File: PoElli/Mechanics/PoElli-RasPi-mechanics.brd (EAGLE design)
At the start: 85 x 56 mm, 30 parts, among them J1 DF12-ELLI-HEADER-TOP, J3 M022.54MM, J4 M022.54MM, T1 Coilcraft 230NL, T2 FLYBACK750311689, U3 FST3257, X1 M-BOLT-2, X2 M-BOLT-2, X3 M-BOLT-2, X4 M-BOLT-2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

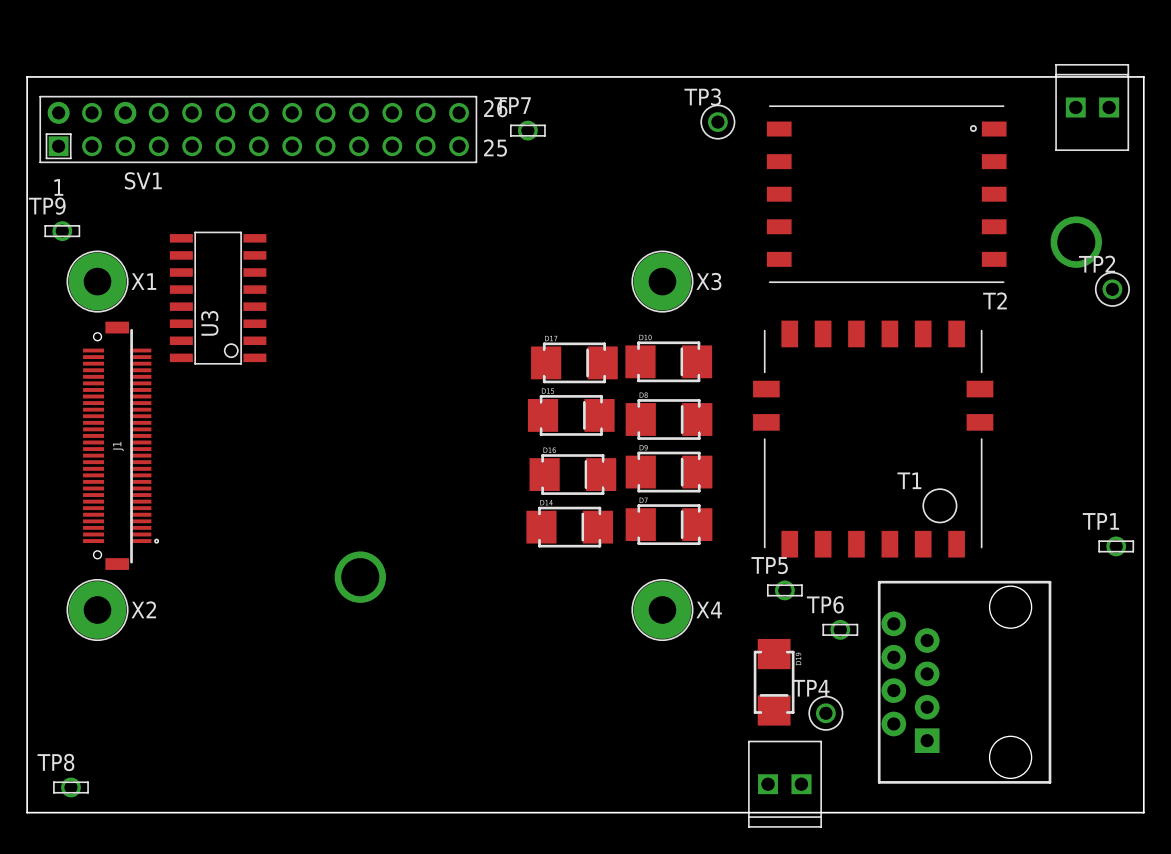
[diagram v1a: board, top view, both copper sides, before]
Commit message: Update RasPi outline & connector
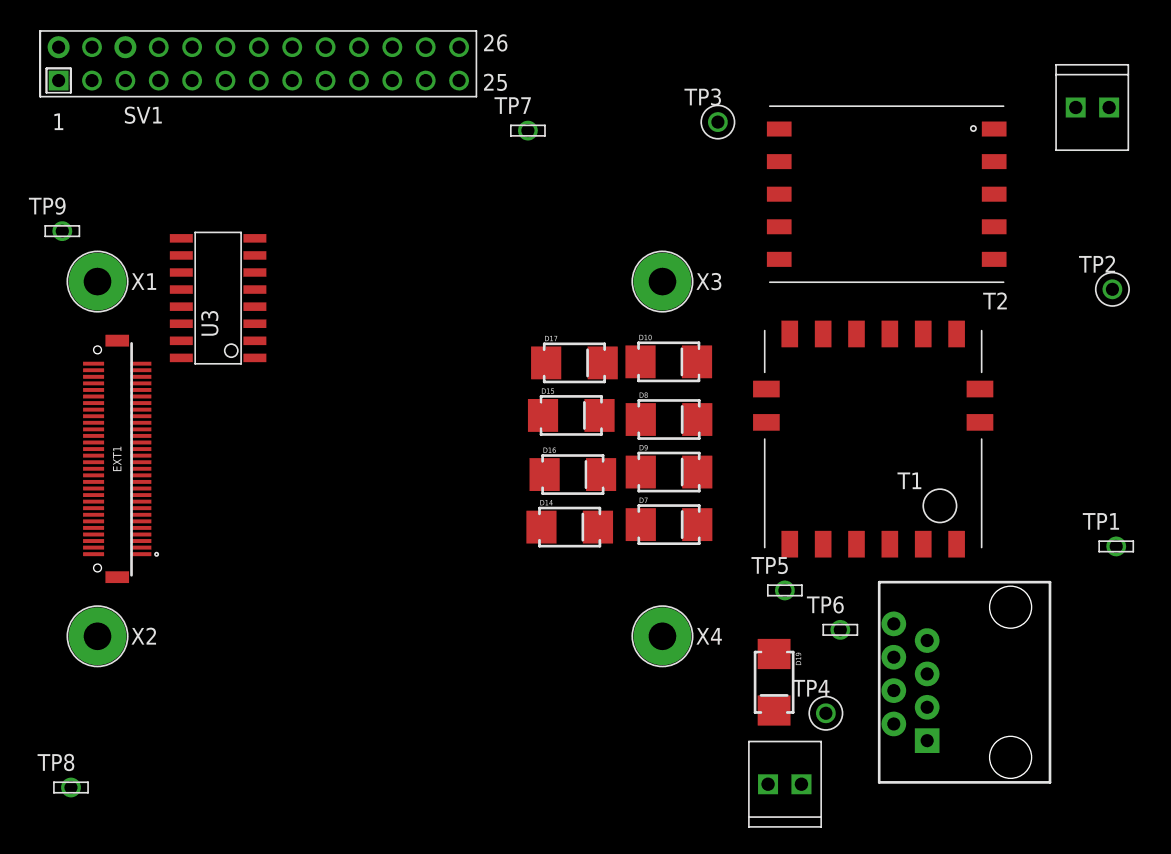
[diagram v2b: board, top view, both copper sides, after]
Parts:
- removed J1: DF12-ELLI-HEADER-TOP, ELL-i-Connectors:DF12(4.0)-60DP-0.5V
- added EXT1: DF12-ELLI-HEADER-TOP, ELL-i-Connectors:DF12(4.0)-60DP-0.5V
- added OUTLINE1: RASPBERRY-OUTLINE, ELL-i-Boards:RASPBERRYPI-SHIELD-OUTLINE
- SV1: value RASPBERRY-SHIELD -> RASPBERRY-CONNECTOR; device ELL-i-Boards:RASPBERRYPI-SHIELD-FULLSIZE -> ELL-i-Boards:RASPBERRYPI-SHIELD-CONNECTOR
- moved SV1 59.8 mm to (17.8, 57.1)
- moved X2 2.00 mm to (5.50, 13.5)
- moved X4 2.00 mm to (48.5, 13.5)
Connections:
- net 3.3V: now also EXT1.6; no longer J1.6
- net 5V: now also EXT1.8; no longer J1.8
- net GND: now also EXT1.12, EXT1.14; no longer J1.12, J1.14
- net VBATT: now also EXT1.4; no longer J1.4
- net VCC(IO): now also EXT1.2; no longer J1.2
- net VIN: now also EXT1.10; no longer J1.10
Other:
- board outline removed
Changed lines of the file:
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@@
 <setting verticaltext="up"/>
 </settings>
-<grid distance="1" unitdist="mm" unit="mm" style="lines" multiple="1" display="no" altdistance="0.5" altunitdist="inch" altunit="mm"/>
+<grid distance="1" unitdist="mm" unit="mm" style="lines" multiple="1" display="no" altdistance="0.1" altunitdist="inch" altunit="inch"/>
 <layers>
 <layer number="1" name="Top" color="4" fill="1" visible="yes" active="yes"/>
@@
 <layer number="111" name="111" color="7" fill="1" visible="yes" active="yes"/>
 <layer number="112" name="tSilk" color="7" fill="1" visible="yes" active="yes"/>
+<layer number="113" name="IDFDebug" color="4" fill="1" visible="yes" active="yes"/>
 <layer number="116" name="Patch_BOT" color="9" fill="4" visible="yes" active="yes"/>
 <layer number="118" name="Rect_Pads" color="7" fill="1" visible="yes" active="yes"/>
@@
 <elements>
 <element name="T1" library="ELL-i-Transformers" package="COILCRAFT-ETH1-230L" value="Coilcraft 230NL" x="64.54" y="28.51" rot="R180"/>
-<element name="SV1" library="ELL-i-Boards" package="RASPBERRYPI-SHIELD-FULLSIZE" value="RASPBERRY-SHIELD" x="0" y="0"/>
-<element name="J1" library="ELL-i-Connectors" package="DF12(4.0)-60DP-0.5V" value="DF12-ELLI-HEADER-TOP" x="7" y="28" rot="R90"/>
+<element name="SV1" library="ELL-i-Boards" package="RASPBERRYPI-SHIELD-CONNECTOR" value="RASPBERRY-CONNECTOR" x="17.78" y="57.07"/>
+<element name="EXT1" library="ELL-i-Connectors" package="DF12(4.0)-60DP-0.5V" value="DF12-ELLI-HEADER-TOP" x="7" y="27" rot="R90"/>
 <element name="D17" library="ELL-i-DIscreteSemi" package="DIODE-B2100" value="B2100" x="41.8" y="34.31"/>
 <element name="D16" library="ELL-i-DIscreteSemi" package="DIODE-B2100" value="B2100" x="41.68" y="25.81"/>
@@
 <element name="D19" library="ELL-i-DIscreteSemi" package="DIODE-B2100" value="B2100" x="57" y="10" rot="R270"/>
 <element name="X1" library="ELL-i-Connectors" package="M2-1" value="M-BOLT-2" x="5.5" y="40.5"/>
-<element name="X2" library="ELL-i-Connectors" package="M2-1" value="M-BOLT-2" x="5.5" y="15.5"/>
+<element name="X2" library="ELL-i-Connectors" package="M2-1" value="M-BOLT-2" x="5.5" y="13.5"/>
 <element name="X3" library="ELL-i-Connectors" package="M2-1" value="M-BOLT-2" x="48.5" y="40.5"/>
-<element name="X4" library="ELL-i-Connectors" package="M2-1" value="M-BOLT-2" x="48.5" y="15.5"/>
+<element name="X4" library="ELL-i-Connectors" package="M2-1" value="M-BOLT-2" x="48.5" y="13.5"/>
 <element name="X5" library="ELL-i-Connectors" package="4UCON-04892" value="POE-TP-RJ45-4UCON" x="75" y="10" rot="R90"/>
+<element name="OUTLINE1" library="ELL-i-Boards" package="RASPBERRYPI-SHIELD-OUTLINE" value="RASPBERRY-OUTLINE" x="0" y="5"/>
 </elements>
 <signals>
 <signal name="VIN">
-<contactref element="J1" pad="10"/>
+<contactref element="EXT1" pad="10"/>
 </signal>
 <signal name="VBATT">
-<contactref element="J1" pad="4"/>
+<contactref element="EXT1" pad="4"/>
 </signal>
 <signal name="N$1">
@@
 </signal>
 <signal name="5V">
-<contactref element="J1" pad="8"/>
+<contactref element="EXT1" pad="8"/>
 <contactref element="SV1" pad="4"/>
 <contactref element="SV1" pad="2"/>
-<wire x1="2.54" y1="53.34" x2="5.08" y2="53.34" width="0" layer="19" extent="1-1"/>
-<wire x1="5.1999" y1="22.25" x2="5.08" y2="53.34" width="0" layer="19" extent="1-1"/>
+<wire x1="2.54" y1="58.34" x2="5.08" y2="58.34" width="0" layer="19" extent="1-1"/>
+<wire x1="5.1999" y1="21.25" x2="5.08" y2="58.34" width="0" layer="19" extent="1-1"/>
 </signal>
 <signal name="POE_A+">
@@
 </signal>
 <signal name="VCC(IO)">
-<contactref element="J1" pad="2"/>
+<contactref element="EXT1" pad="2"/>
 </signal>
 <signal name="GND">
-<contactref element="J1" pad="14"/>
-<contactref element="J1" pad="12"/>
+<contactref element="EXT1" pad="14"/>
+<contactref element="EXT1" pad="12"/>
 <contactref element="U3" pad="8"/>
 <contactref element="SV1" pad="9"/>
@@
 <contactref element="SV1" pad="14"/>
 <contactref element="SV1" pad="6"/>
-<wire x1="25.4" y1="53.34" x2="33.02" y2="50.8" width="0" layer="19" extent="1-1"/>
-<wire x1="17.78" y1="53.34" x2="25.4" y2="53.34" width="0" layer="19" extent="1-1"/>
-<wire x1="12.7" y1="50.8" x2="17.78" y2="53.34" width="0" layer="19" extent="1-1"/>
-<wire x1="7.62" y1="53.34" x2="12.7" y2="50.8" width="0" layer="19" extent="1-1"/>
-<wire x1="17.48" y1="43.79" x2="12.7" y2="50.8" width="0" layer="19" extent="1-1"/>
-<wire x1="5.1999" y1="23.75" x2="17.48" y2="43.79" width="0" layer="19" extent="1-1"/>
-<wire x1="5.1999" y1="23.25" x2="5.1999" y2="23.75" width="0" layer="19" extent="1-1"/>
+<wire x1="25.4" y1="58.34" x2="33.02" y2="55.8" width="0" layer="19" extent="1-1"/>
+<wire x1="17.78" y1="58.34" x2="25.4" y2="58.34" width="0" layer="19" extent="1-1"/>
+<wire x1="12.7" y1="55.8" x2="17.78" y2="58.34" width="0" layer="19" extent="1-1"/>
+<wire x1="7.62" y1="58.34" x2="12.7" y2="55.8" width="0" layer="19" extent="1-1"/>
+<wire x1="17.48" y1="43.79" x2="12.7" y2="55.8" width="0" layer="19" extent="1-1"/>
+<wire x1="5.1999" y1="22.75" x2="17.48" y2="43.79" width="0" layer="19" extent="1-1"/>
+<wire x1="5.1999" y1="22.25" x2="5.1999" y2="22.75" width="0" layer="19" extent="1-1"/>
 </signal>
 <signal name="3.3V">
-<contactref element="J1" pad="6"/>
+<contactref element="EXT1" pad="6"/>
 <contactref element="SV1" pad="1"/>
 <contactref element="SV1" pad="17"/>
-<wire x1="2.54" y1="50.8" x2="22.86" y2="50.8" width="0" layer="19" extent="1-1"/>
-<wire x1="5.1999" y1="21.75" x2="2.54" y2="50.8" width="0" layer="19" extent="1-1"/>
+<wire x1="2.54" y1="55.8" x2="22.86" y2="55.8" width="0" layer="19" extent="1-1"/>
+<wire x1="5.1999" y1="20.75" x2="2.54" y2="55.8" width="0" layer="19" extent="1-1"/>
 </signal>
 <signal name="VCC">
